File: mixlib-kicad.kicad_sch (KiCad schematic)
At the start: 47 parts, among them Q1 MMBT5551L, Q2 MMBT5551L, Q3 PMD3001D, Q4 PBSS4160DS, Q6 PBSS4160DPN, U1 ADA4522-4, U2 MCP6404, U3 ADA4522-2, U4 LM4040DBZ-10, U5 TPS5430DDA

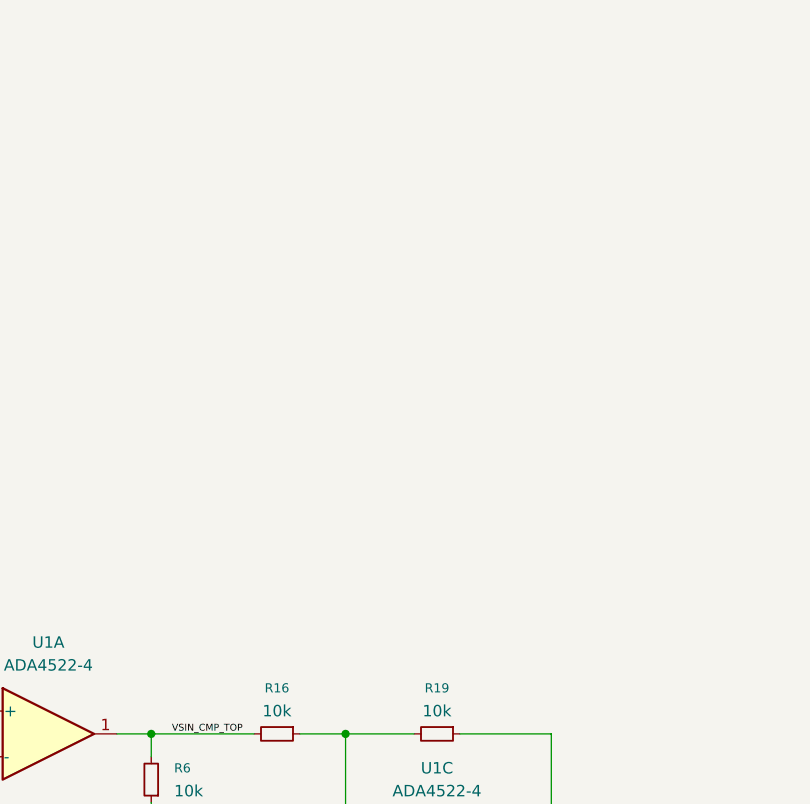
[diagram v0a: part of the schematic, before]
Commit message: refactor(pmic-switch): TPS2121: reposition symbol pins
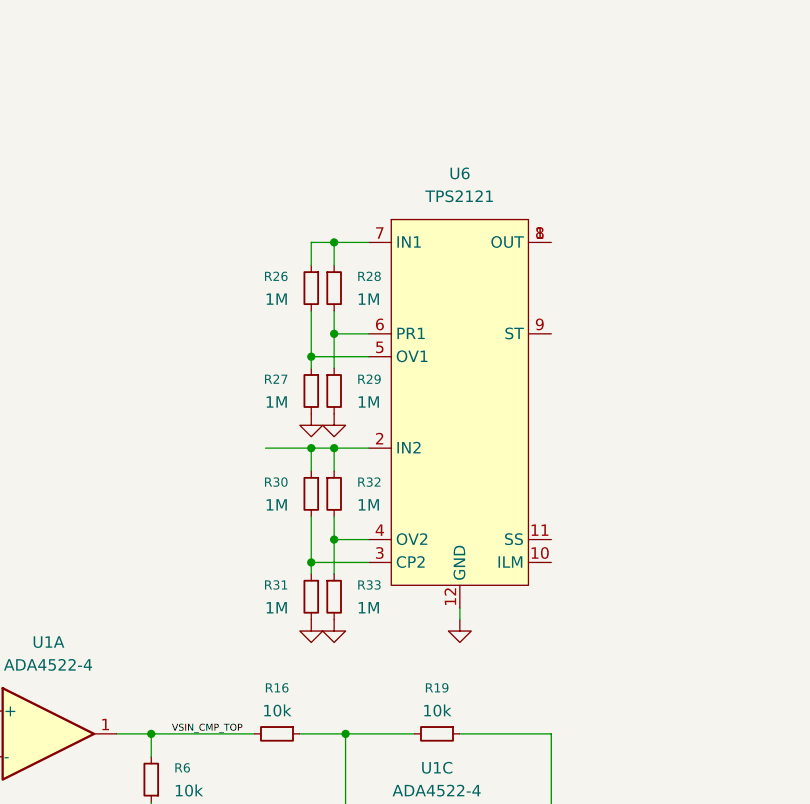
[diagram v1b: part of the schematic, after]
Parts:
- added R26, R27, R28, R29, R30, R31, R32, R33: 1M, symbol Device:R_Small
- added U6: TPS2121, mixlib-vendor-ti:vendor-ti-RUX0012A, symbol mixlib-pmic-switch:TPS2121
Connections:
- net GND: now also R27.2, R29.2, R31.2, R33.2, U6.12 (GND)
- new net: R32.2, R33.1, U6.4 (OV2)
- new net: R26.2, R27.1, U6.5 (OV1)
- new net: R30.1, R32.1, U6.2 (IN2)
- new net: R26.1, R28.1, U6.7 (IN1)
- new net: R30.2, R31.1, U6.3 (CP2)
- new net: R28.2, R29.1, U6.6 (PR1)
- new net: U6.1 (OUT), U6.8 (OUT)

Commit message: feat(discrete-led): add generic Aliexpress 0603 discrete LED
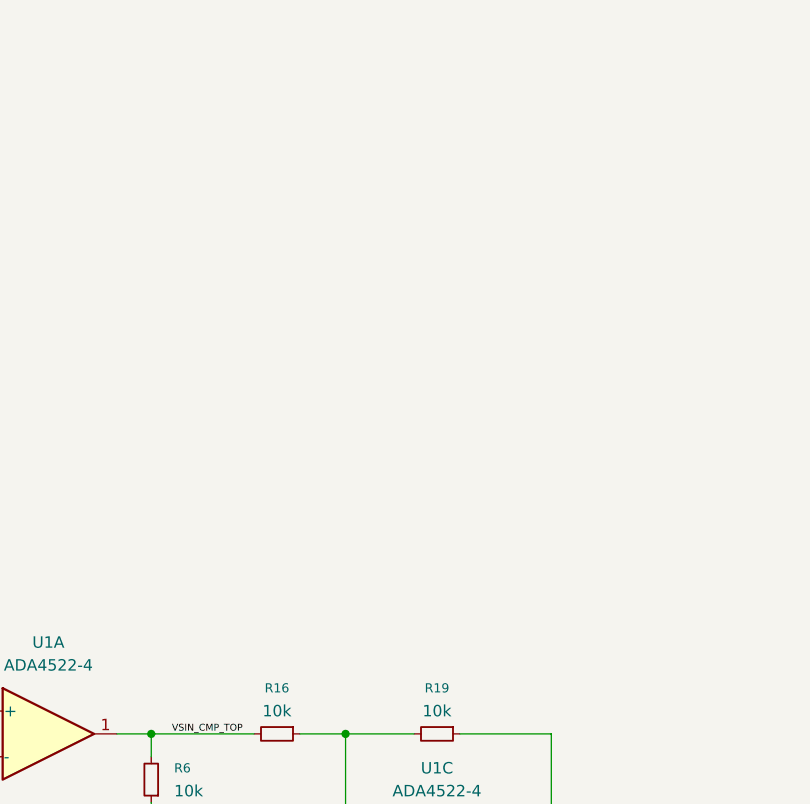
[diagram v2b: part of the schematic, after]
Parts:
- removed R26, R27, R28, R29, R30, R31, R32, R33: 1M, symbol Device:R_Small
- removed U6: TPS2121, mixlib-vendor-ti:vendor-ti-RUX0012A, symbol mixlib-pmic-switch:TPS2121

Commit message: refactor(discrete-led): rearrange generic Aliexpress 0603 discrete LED symbol
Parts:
- added R26, R27, R28: R_Small, symbol Device:R_Small
- added U6: TJ-S1615CY6TGLCCYRGY-A5, mixlib-discrete-led:LED-3_RGB-0603_1615Metric, symbol mixlib-discrete-led:TJ-S1615CY6TGLCCYRGY-A5
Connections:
- new net: R28.2, U6.4 (R)
- new net: R26.2, U6.2 (Y)
- new net: R27.2, U6.3 (G)

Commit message: feat(ic-mcu): add CH32V/CH32F MCUs
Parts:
- added U7: CH32V006K8U6, Package_DFN_QFN:QFN-32-1EP_4x4mm_P0.4mm_EP2.9x2.9mm, symbol mixlib-ic-mcu:CH32V006K8U6
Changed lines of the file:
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@@
+	)
+	(symbol
+		(lib_id "mixlib-ic-mcu:CH32V006K8U6")
+		(at 369.57 -21.59 0)
+		(unit 1)
+		(body_style 1)
+		(exclude_from_sim no)
+		(in_bom yes)
+		(on_board yes)
+		(in_pos_files yes)
+		(dnp no)
+		(fields_autoplaced yes)
+		(property "Reference" "U7"
+			(at 371.7133 -49.53 0)
+			(show_name no)
+			(do_not_autoplace no)
+			(effects
+				(font
+					(size 1.27 1.27)
+				)
+				(justify left)
+			)
+		)
+		(property "Value" "CH32V006K8U6"
+			(at 371.7133 -46.99 0)
+			(show_name no)
+			(do_not_autoplace no)
+			(effects
+				(font
+					(size 1.27 1.27)
+				)
+				(justify left)
+			)
+		)
+		(property "Footprint" "Package_DFN_QFN:QFN-32-1EP_4x4mm_P0.4mm_EP2.9x2.9mm"
+			(at 368.808 29.21 0)
+			(hide yes)
+			(show_name no)
+			(do_not_autoplace no)
+			(effects
+				(font
+					(size 1.27 1.27)
+				)
+			)
+		)
+		(property "Datasheet" "https://ch32-riscv-ug.github.io/CH32V006/datasheet_en/CH32V006DS0.PDF"
+			(at 368.808 29.21 0)
+			(hide yes)
+			(show_name no)
+			(do_not_autoplace no)
+			(effects
+				(font
+					(size 1.27 1.27)
+				)
+			)
+		)
+		(property "Description" "48MHz RISC-V MCU, 8KB RAM, 62KB Flash, QFN-32"
+			(at 368.808 29.21 0)
+			(hide yes)
+			(show_name no)
+			(do_not_autoplace no)
+			(effects
+				(font
+					(size 1.27 1.27)
+				)
+			)
+		)
+		(pin "5"
+		)
+		(pin "4"
+		)
+		(pin "6"
+		)
+		(pin "32"
+		)
+		(pin "8"
+		)
+		(pin "9"
+		)
+		(pin "33"
+		)
+		(pin "24"
+		)
+		(pin "15"
+		)
+		(pin "10"
+		)
+		(pin "23"
+		)
+		(pin "17"
+		)
+		(pin "21"
+		)
+		(pin "11"
+		)
+		(pin "25"
+		)
+		(pin "14"
+		)
+		(pin "13"
+		)
+		(pin "16"
+		)
+		(pin "18"
+		)
+		(pin "19"
+		)
+		(pin "20"
+		)
+		(pin "26"
+		)
+		(pin "12"
+		)
+		(pin "22"
+		)
+		(pin "31"
+		)
+		(pin "1"
+		)
+		(pin "29"
+		)
+		(pin "7"
+		)
+		(pin "2"
+		)
+		(pin "27"
+		)
+		(pin "30"
+		)
+		(pin "3"
+		)
+		(pin "28"
+		)
+		(instances
+			(project "mixlib-kicad"
+				(path "/addedff5-7d4f-4971-a0ac-6e5a34b85b52"
+					(reference "U7")
+					(unit 1)
+				)
+			)
+		)
 	)
 	(symbol
